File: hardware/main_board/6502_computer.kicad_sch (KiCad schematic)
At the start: 54 parts, among them J1 Conn_02x20_Odd_Even, J2 Conn_01x40_Socket, J3 Conn_01x40_Socket, J4 Conn_01x02_Pin, J6 DE9_Pins, J7 Mini-DIN-6, J8 Conn_01x12_Pin, SW1 SW_Push, U1 6502, U11 74HC595, U12 74HC138, U13 6522, U15 MAX232, U16 6551, U17 74HC595, U18 74HC14, U4 HM62256BLP, U8 74HC00, U9 28C256, Y1 CXO_DIP8, Y3 1.8432MHz

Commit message: Adds stuff
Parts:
- J6: footprint Connector_Dsub:DSUB-9_Pins_Horizontal_P2.77x2.84mm_EdgePinOffset7.70mm_Housed_MountingHolesOffset9.12mm -> Connector_Dsub:DSUB-9_Socket_Horizontal_P2.77x2.84mm_EdgePinOffset7.70mm_Housed_MountingHolesOffset9.12mm
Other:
- note added: "!!!!!!!!!CS2B!!!!!!!!"
- note added: "!!!!!!!!!RESB!!!!!!!!"
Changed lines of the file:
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@@
 		(rev "0")
 	)
+	(text "!!!!!!!!!CS2B!!!!!!!!"
+		(exclude_from_sim no)
+		(at 381.254 186.182 0)
+		(effects
+			(font
+				(size 2.54 2.54)
+				(thickness 0.254)
+				(bold yes)
+			)
+		)
+	)
 	(text "UART"
 		(exclude_from_sim no)
@@
 	(text "Keyboard \nlogic"
 		(exclude_from_sim no)
-		(at 281.94 214.376 0)
+		(at 284.226 217.17 0)
+		(effects
+			(font
+				(size 2.54 2.54)
+			)
+		)
+	)
+	(text "!!!!!!!!!RESB!!!!!!!!"
+		(exclude_from_sim no)
+		(at 345.44 46.228 0)
 		(effects
 			(font
 				(size 2.54 2.54)
+				(thickness 0.254)
+				(bold yes)
 			)
 		)
@@
 			)
 		)
-		(property "Footprint" "Connector_Dsub:DSUB-9_Pins_Horizontal_P2.77x2.84mm_EdgePinOffset7.70mm_Housed_MountingHolesOffset9.12mm"
+		(property "Footprint" "Connector_Dsub:DSUB-9_Socket_Horizontal_P2.77x2.84mm_EdgePinOffset7.70mm_Housed_MountingHolesOffset9.12mm"
 			(at 273.05 20.32 0)
 			(effects

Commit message: updated readme
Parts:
- R1, R2, R3, R6, R7, R8: footprint Resistor_THT:R_Axial_DIN0207_L6.3mm_D2.5mm_P7.62mm_Horizontal -> Resistor_THT:R_Axial_DIN0207_L6.3mm_D2.5mm_P10.16mm_Horizontal
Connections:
- net GND: no longer J1.2 (Pin_2), J1.31 (Pin_31), J2.2 (Pin_2), J2.37 (Pin_37), J2.38 (Pin_38), J3.2 (Pin_2), J3.37 (Pin_37), J3.38 (Pin_38)
- no-connect marks 40 -> 48
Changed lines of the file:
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@@
 	)
 	(junction
-		(at 106.68 265.43)
-		(diameter 0)
-		(color 0 0 0 0)
-	)
-	(junction
 		(at 270.51 161.29)
 		(diameter 0)
@@
 	)
 	(junction
-		(at 152.4 175.26)
-		(diameter 0)
-		(color 0 0 0 0)
-	)
-	(junction
 		(at 236.22 86.36)
 		(diameter 0)
@@
 	)
 	(junction
-		(at 106.68 267.97)
-		(diameter 0)
-		(color 0 0 0 0)
-	)
-	(junction
 		(at 161.29 49.53)
 		(diameter 0)
@@
 	)
 	(junction
-		(at 106.68 176.53)
-		(diameter 0)
-		(color 0 0 0 0)
-	)
-	(junction
 		(at 292.1 78.74)
 		(diameter 0)
@@
 	)
 	(junction
-		(at 77.47 176.53)
-		(diameter 0)
-		(color 0 0 0 0)
-	)
-	(junction
 		(at 229.87 144.78)
 		(diameter 0)
@@
 	)
 	(junction
-		(at 152.4 214.63)
-		(diameter 0)
-		(color 0 0 0 0)
-	)
-	(junction
 		(at 72.39 31.75)
 		(diameter 0)
@@
 	)
 	(junction
-		(at 77.47 267.97)
-		(diameter 0)
-		(color 0 0 0 0)
-	)
-	(junction
-		(at 77.47 265.43)
-		(diameter 0)
-		(color 0 0 0 0)
-	)
-	(junction
 		(at 39.37 116.84)
 		(diameter 0)
@@
 	)
 	(no_connect
+		(at 106.68 179.07)
+	)
+	(no_connect
 		(at 280.67 151.13)
 	)
@@
 	)
 	(no_connect
+		(at 106.68 270.51)
+	)
+	(no_connect
 		(at 74.93 134.62)
 	)
@@
 	)
 	(no_connect
+		(at 77.47 267.97)
+	)
+	(no_connect
 		(at 275.59 27.94)
 	)
@@
 	)
 	(no_connect
+		(at 152.4 217.17)
+	)
+	(no_connect
 		(at 77.47 273.05)
 	)
 	(no_connect
+		(at 77.47 270.51)
+	)
+	(no_connect
 		(at 71.12 68.58)
 	)
@@
 	)
 	(no_connect
+		(at 106.68 267.97)
+	)
+	(no_connect
 		(at 207.01 223.52)
 	)
 	(no_connect
+		(at 165.1 179.07)
+	)
+	(no_connect
 		(at 377.19 238.76)
 	)
+	(no_connect
+		(at 77.47 179.07)
+	)
 	(bus_entry
 		(at 377.19 160.02)
@@
 		)
 	)
-	(wire
-		(pts
-			(xy 106.68 265.43) (xy 106.68 267.97)
-		)
-		(stroke
-			(width 0)
-			(type default)
-		)
-	)
 	(bus
 		(pts
@@
 		)
 	)
-	(wire
-		(pts
-			(xy 152.4 214.63) (xy 152.4 217.17)
-		)
-		(stroke
-			(width 0)
-			(type default)
-		)
-	)
 	(bus
 		(pts
@@
 	(wire
 		(pts
-			(xy 165.1 179.07) (xy 165.1 175.26)
-		)
-		(stroke
-			(width 0)
-			(type default)
-		)
-	)
-	(wire
-		(pts
 			(xy 217.17 204.47) (xy 179.07 204.47)
 		)
@@
 	(wire
 		(pts
-			(xy 77.47 173.99) (xy 77.47 176.53)
-		)
-		(stroke
-			(width 0)
-			(type default)
-		)
-	)
-	(wire
-		(pts
 			(xy 330.2 67.31) (xy 341.63 67.31)
 		)
@@
 	(wire
 		(pts
-			(xy 106.68 267.97) (xy 106.68 270.51)
-		)
-		(stroke
-			(width 0)
-			(type default)
-		)
-	)
-	(wire
-		(pts
 			(xy 36.83 93.98) (xy 48.26 93.98)
 		)
@@
 	(wire
 		(pts
-			(xy 77.47 267.97) (xy 77.47 270.51)
-		)
-		(stroke
-			(width 0)
-			(type default)
-		)
-	)
-	(wire
-		(pts
 			(xy 100.33 255.27) (xy 106.68 255.27)
 		)
@@
 	(wire
 		(pts
-			(xy 100.33 270.51) (xy 100.33 275.59)
+			(xy 100.33 274.32) (xy 100.33 275.59)
 		)
 		(stroke
@@
 		)
 	)
-	(bus
+	(wire
 		(pts
-			(xy 344.17 72.39) (xy 344.17 74.93)
+			(xy 106.68 173.99) (xy 106.68 176.53)
 		)
 		(stroke
@@
 		)
 	)
-	(wire
+	(bus
 		(pts
-			(xy 187.96 147.32) (xy 194.31 147.32)
+			(xy 344.17 72.39) (xy 344.17 74.93)
 		)
 		(stroke
@@
 	(wire
 		(pts
-			(xy 259.08 128.27) (xy 270.51 128.27)
+			(xy 187.96 147.32) (xy 194.31 147.32)
 		)
 		(stroke
@@
 	(wire
 		(pts
-			(xy 229.87 130.81) (xy 229.87 133.35)
+			(xy 259.08 128.27) (xy 270.51 128.27)
 		)
 		(stroke
@@
 	(wire
 		(pts
-			(xy 106.68 173.99) (xy 106.68 176.53)
+			(xy 229.87 130.81) (xy 229.87 133.35)
 		)
 		(stroke
@@
 	(wire
 		(pts
+			(xy 77.47 173.99) (xy 77.47 176.53)
+		)
+		(stroke
+			(width 0)
+			(type default)
+		)
+	)
+	(wire
+		(pts
 			(xy 67.31 204.47) (xy 77.47 204.47)
 		)
@@
 	(wire
 		(pts
-			(xy 77.47 176.53) (xy 77.47 179.07)
-		)
-		(stroke
-			(width 0)
-			(type default)
-		)
-	)
-	(wire
-		(pts
 			(xy 236.22 86.36) (xy 257.81 86.36)
 		)
@@
 	(wire
 		(pts
-			(xy 106.68 176.53) (xy 106.68 179.07)
-		)
-		(stroke
-			(width 0)
-			(type default)
-		)
-	)
-	(wire
-		(pts
 			(xy 224.79 226.06) (xy 224.79 237.49)
 		)
@@
 	(wire
 		(pts
-			(xy 77.47 265.43) (xy 77.47 267.97)
-		)
-		(stroke
-			(width 0)
-			(type default)
-		)
-	)
-	(wire
-		(pts
 			(xy 148.59 102.87) (xy 148.59 110.49)
 		)
@@
 		)
 	)
-	(wire
-		(pts
-			(xy 152.4 175.26) (xy 165.1 175.26)
-		)
-		(stroke
-			(width 0)
-			(type default)
-		)
-	)
 	(bus
 		(pts
@@
 			)
 		)
-		(property "Footprint" "Resistor_THT:R_Axial_DIN0207_L6.3mm_D2.5mm_P7.62mm_Horizontal"
+		(property "Footprint" "Resistor_THT:R_Axial_DIN0207_L6.3mm_D2.5mm_P10.16mm_Horizontal"
 			(at 40.132 55.88 90)
 			(effects
@@
 			)
 		)
-		(property "Footprint" "Resistor_THT:R_Axial_DIN0207_L6.3mm_D2.5mm_P7.62mm_Horizontal"
+		(property "Footprint" "Resistor_THT:R_Axial_DIN0207_L6.3mm_D2.5mm_P10.16mm_Horizontal"
 			(at 19.812 55.88 90)
 			(effects
@@
 			)
 		)
-		(property "Footprint" "Resistor_THT:R_Axial_DIN0207_L6.3mm_D2.5mm_P7.62mm_Horizontal"
+		(property "Footprint" "Resistor_THT:R_Axial_DIN0207_L6.3mm_D2.5mm_P10.16mm_Horizontal"
 			(at 29.972 55.88 90)
 			(effects
@@
 			)
 		)
-		(property "Footprint" "Resistor_THT:R_Axial_DIN0207_L6.3mm_D2.5mm_P7.62mm_Horizontal"
+		(property "Footprint" "Resistor_THT:R_Axial_DIN0207_L6.3mm_D2.5mm_P10.16mm_Horizontal"
 			(at 98.552 29.21 90)
 			(effects
@@
 			)
 		)
-		(property "Footprint" "Resistor_THT:R_Axial_DIN0207_L6.3mm_D2.5mm_P7.62mm_Horizontal"
+		(property "Footprint" "Resistor_THT:R_Axial_DIN0207_L6.3mm_D2.5mm_P10.16mm_Horizontal"
 			(at 45.212 27.94 90)
 			(effects
@@
 	(symbol
 		(lib_id "power:VDD")
-		(at 100.33 270.51 0)
+		(at 100.33 274.32 0)
 		(unit 1)
 		(exclude_from_sim no)
@@
 		(dnp no)
 		(property "Reference" "#PWR045"
-			(at 100.33 274.32 0)
+			(at 100.33 278.13 0)
 			(effects
 				(font
@@
 		)
 		(property "Value" "VDD"
-			(at 97.282 270.002 0)
+			(at 97.282 273.812 0)
 			(effects
 				(font
@@
 		)
 		(property "Footprint" ""
-			(at 100.33 270.51 0)
+			(at 100.33 274.32 0)
 			(effects
 				(font
@@
 		)
 		(property "Datasheet" ""
-			(at 100.33 270.51 0)
+			(at 100.33 274.32 0)
 			(effects
 				(font
@@
 		)
 		(property "Description" "Power symbol creates a global label with name \"VDD\""
-			(at 100.33 270.51 0)
+			(at 100.33 274.32 0)
 			(effects
 				(font
@@
 			)
 		)
-		(property "Footprint" "Resistor_THT:R_Axial_DIN0207_L6.3mm_D2.5mm_P7.62mm_Horizontal"
+		(property "Footprint" "Resistor_THT:R_Axial_DIN0207_L6.3mm_D2.5mm_P10.16mm_Horizontal"
 			(at 248.92 227.838 90)
 			(effects

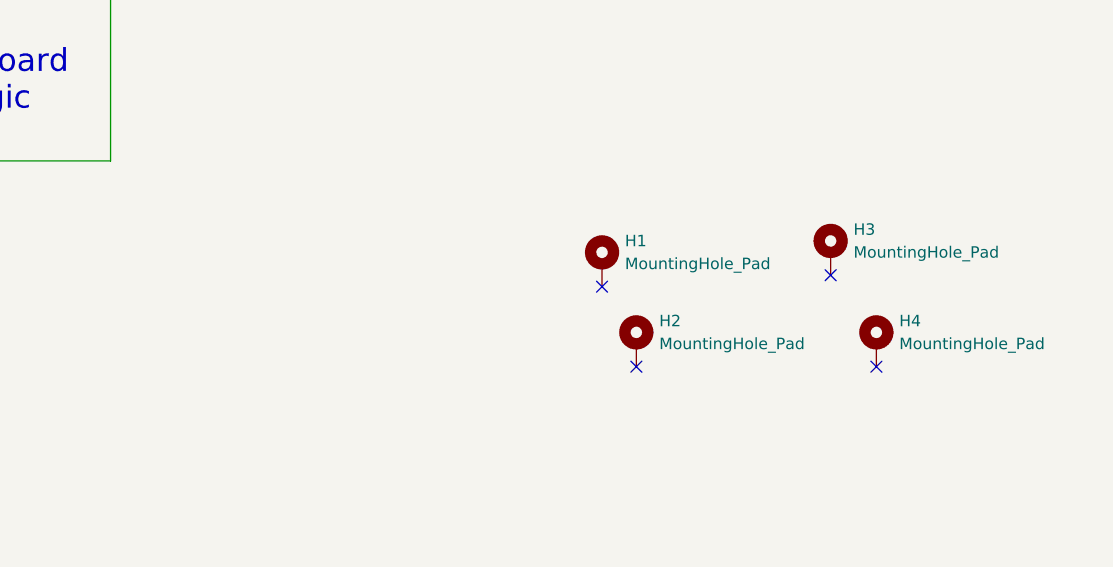
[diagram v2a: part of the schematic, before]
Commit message: replace load with rx
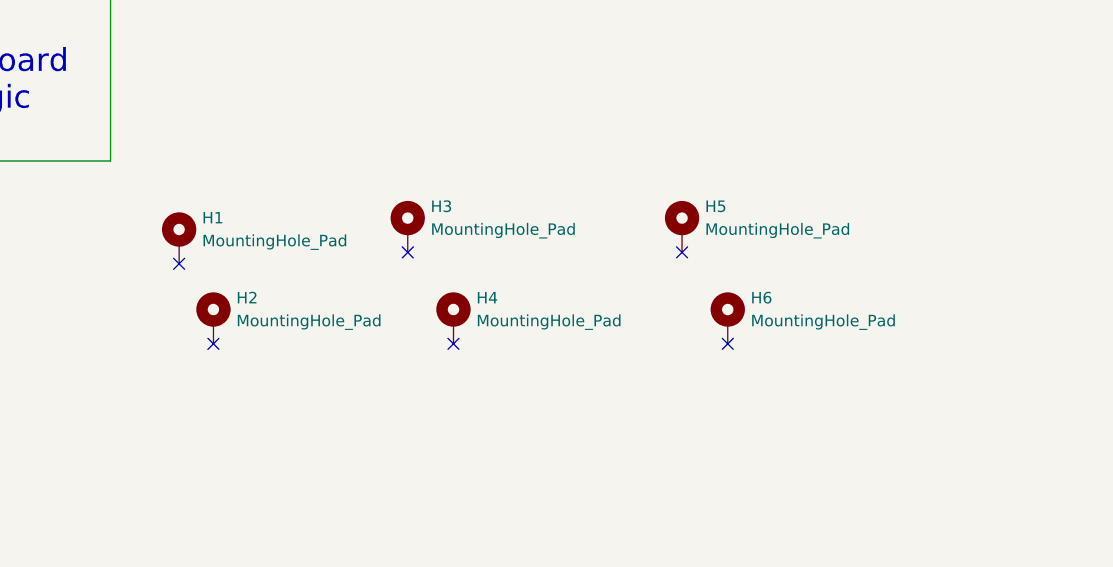
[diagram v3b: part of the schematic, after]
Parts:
- added H5, H6: MountingHole_Pad, MountingHole:MountingHole_3.2mm_M3_ISO7380_Pad, symbol Mechanical:MountingHole_Pad
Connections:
- no-connect marks 48 -> 50
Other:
- moved on the sheet: H1, H2, H3, H4
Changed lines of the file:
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@@
 	)
 	(no_connect
-		(at 351.79 240.03)
+		(at 304.8 237.49)
 	)
 	(no_connect
@@
 	)
 	(no_connect
-		(at 355.6 248.92)
+		(at 308.61 246.38)
 	)
 	(no_connect
@@
 	)
 	(no_connect
+		(at 360.68 236.22)
+	)
+	(no_connect
 		(at 152.4 219.71)
 	)
@@
 	)
 	(no_connect
+		(at 365.76 246.38)
+	)
+	(no_connect
 		(at 48.26 68.58)
 	)
@@
 	)
 	(no_connect
-		(at 382.27 248.92)
+		(at 335.28 246.38)
 	)
 	(no_connect
@@
 	)
 	(no_connect
-		(at 377.19 238.76)
+		(at 330.2 236.22)
 	)
 	(no_connect
@@
 	)
 	(symbol
+		(lib_id "Mechanical:MountingHole_Pad")
+		(at 360.68 233.68 0)
+		(unit 1)
+		(exclude_from_sim no)
+		(in_bom no)
+		(on_board yes)
+		(dnp no)
+		(fields_autoplaced yes)
+		(property "Reference" "H5"
+			(at 363.22 231.1399 0)
+			(effects
+				(font
+					(size 1.27 1.27)
+				)
+				(justify left)
+			)
+		)
+		(property "Value" "MountingHole_Pad"
+			(at 363.22 233.6799 0)
+			(effects
+				(font
+					(size 1.27 1.27)
+				)
+				(justify left)
+			)
+		)
+		(property "Footprint" "MountingHole:MountingHole_3.2mm_M3_ISO7380_Pad"
+			(at 360.68 233.68 0)
+			(effects
+				(font
+					(size 1.27 1.27)
+				)
+				(hide yes)
+			)
+		)
+		(property "Datasheet" "~"
+			(at 360.68 233.68 0)
+			(effects
+				(font
+					(size 1.27 1.27)
+				)
+				(hide yes)
+			)
+		)
+		(property "Description" "Mounting Hole with connection"
+			(at 360.68 233.68 0)
+			(effects
+				(font
+					(size 1.27 1.27)
+				)
+				(hide yes)
+			)
+		)
+		(pin "1"
+		)
+		(instances
+			(project "6502_computer"
+				(path "/12aa21c8-f5ca-498b-99d6-b9ebca65be14"
+					(reference "H5")
+					(unit 1)
+				)
+			)
+		)
+	)
+	(symbol
 		(lib_id "power:GND")
 		(at 140.97 175.26 0)
@@
 	(symbol
 		(lib_id "Mechanical:MountingHole_Pad")
-		(at 382.27 246.38 0)
+		(at 335.28 243.84 0)
 		(unit 1)
 		(exclude_from_sim no)
@@
 		(fields_autoplaced yes)
 		(property "Reference" "H4"
-			(at 384.81 243.8399 0)
+			(at 337.82 241.2999 0)
 			(effects
 				(font
@@
 		)
 		(property "Value" "MountingHole_Pad"
-			(at 384.81 246.3799 0)
+			(at 337.82 243.8399 0)
 			(effects
 				(font
@@
 		)
 		(property "Footprint" "MountingHole:MountingHole_3.2mm_M3_ISO7380_Pad"
-			(at 382.27 246.38 0)
+			(at 335.28 243.84 0)
 			(effects
 				(font
@@
 		)
 		(property "Datasheet" "~"
-			(at 382.27 246.38 0)
+			(at 335.28 243.84 0)
 			(effects
 				(font
@@
 		)
 		(property "Description" "Mounting Hole with connection"
-			(at 382.27 246.38 0)
+			(at 335.28 243.84 0)
 			(effects
 				(font
@@
 	(symbol
 		(lib_id "Mechanical:MountingHole_Pad")
-		(at 377.19 236.22 0)
+		(at 330.2 233.68 0)
 		(unit 1)
 		(exclude_from_sim no)
@@
 		(fields_autoplaced yes)
 		(property "Reference" "H3"
-			(at 379.73 233.6799 0)
+			(at 332.74 231.1399 0)
 			(effects
 				(font
@@
 		)
 		(property "Value" "MountingHole_Pad"
-			(at 379.73 236.2199 0)
+			(at 332.74 233.6799 0)
 			(effects
 				(font
@@
 		)
 		(property "Footprint" "MountingHole:MountingHole_3.2mm_M3_ISO7380_Pad"
-			(at 377.19 236.22 0)
+			(at 330.2 233.68 0)
 			(effects
 				(font
@@
 		)
 		(property "Datasheet" "~"
-			(at 377.19 236.22 0)
+			(at 330.2 233.68 0)
 			(effects
 				(font
@@
 		)
 		(property "Description" "Mounting Hole with connection"
-			(at 377.19 236.22 0)
+			(at 330.2 233.68 0)
 			(effects
 				(font
@@
 	(symbol
 		(lib_id "Mechanical:MountingHole_Pad")
-		(at 351.79 237.49 0)
+		(at 304.8 234.95 0)
 		(unit 1)
 		(exclude_from_sim no)
@@
 		(fields_autoplaced yes)
 		(property "Reference" "H1"
-			(at 354.33 234.9499 0)
+			(at 307.34 232.4099 0)
 			(effects
 				(font
@@
 		)
 		(property "Value" "MountingHole_Pad"
-			(at 354.33 237.4899 0)
+			(at 307.34 234.9499 0)
 			(effects
 				(font
@@
 		)
 		(property "Footprint" "MountingHole:MountingHole_3.2mm_M3_ISO7380_Pad"
-			(at 351.79 237.49 0)
+			(at 304.8 234.95 0)
 			(effects
 				(font
@@
 		)
 		(property "Datasheet" "~"
-			(at 351.79 237.49 0)
+			(at 304.8 234.95 0)
 			(effects
 				(font
@@
 		)
 		(property "Description" "Mounting Hole with connection"
-			(at 351.79 237.49 0)
+			(at 304.8 234.95 0)
 			(effects
 				(font
@@
 	)
 	(symbol
+		(lib_id "Mechanical:MountingHole_Pad")
+		(at 365.76 243.84 0)
+		(unit 1)
+		(exclude_from_sim no)
+		(in_bom no)
+		(on_board yes)
+		(dnp no)
+		(fields_autoplaced yes)
+		(property "Reference" "H6"
+			(at 368.3 241.2999 0)
+			(effects
+				(font
+					(size 1.27 1.27)
+				)
+				(justify left)
+			)
+		)
+		(property "Value" "MountingHole_Pad"
+			(at 368.3 243.8399 0)
+			(effects
+				(font
+					(size 1.27 1.27)
+				)
+				(justify left)
+			)
+		)
+		(property "Footprint" "MountingHole:MountingHole_3.2mm_M3_ISO7380_Pad"
+			(at 365.76 243.84 0)
+			(effects
+				(font
+					(size 1.27 1.27)
+				)
+				(hide yes)
+			)
+		)
+		(property "Datasheet" "~"
+			(at 365.76 243.84 0)
+			(effects
+				(font
+					(size 1.27 1.27)
+				)
+				(hide yes)
+			)
+		)
+		(property "Description" "Mounting Hole with connection"
+			(at 365.76 243.84 0)
+			(effects
+				(font
+					(size 1.27 1.27)
+				)
+				(hide yes)
+			)
+		)
+		(pin "1"
+		)
+		(instances
+			(project "6502_computer"
+				(path "/12aa21c8-f5ca-498b-99d6-b9ebca65be14"
+					(reference "H6")
+					(unit 1)
+				)
+			)
+		)
+	)
+	(symbol
 		(lib_id "power:GND")
 		(at 72.39 34.29 0)
@@
 	(symbol
 		(lib_id "Mechanical:MountingHole_Pad")
-		(at 355.6 246.38 0)
+		(at 308.61 243.84 0)
 		(unit 1)
 		(exclude_from_sim no)
@@
 		(fields_autoplaced yes)
 		(property "Reference" "H2"
-			(at 358.14 243.8399 0)
+			(at 311.15 241.2999 0)
 			(effects
 				(font
@@
 		)
 		(property "Value" "MountingHole_Pad"
-			(at 358.14 246.3799 0)
+			(at 311.15 243.8399 0)
 			(effects
 				(font
@@
 		)
 		(property "Footprint" "MountingHole:MountingHole_3.2mm_M3_ISO7380_Pad"
-			(at 355.6 246.38 0)
+			(at 308.61 243.84 0)
 			(effects
 				(font
@@
 		)
 		(property "Datasheet" "~"
-			(at 355.6 246.38 0)
+			(at 308.61 243.84 0)
 			(effects
 				(font
@@
 		)
 		(property "Description" "Mounting Hole with connection"
-			(at 355.6 246.38 0)
+			(at 308.61 243.84 0)
 			(effects
 				(font

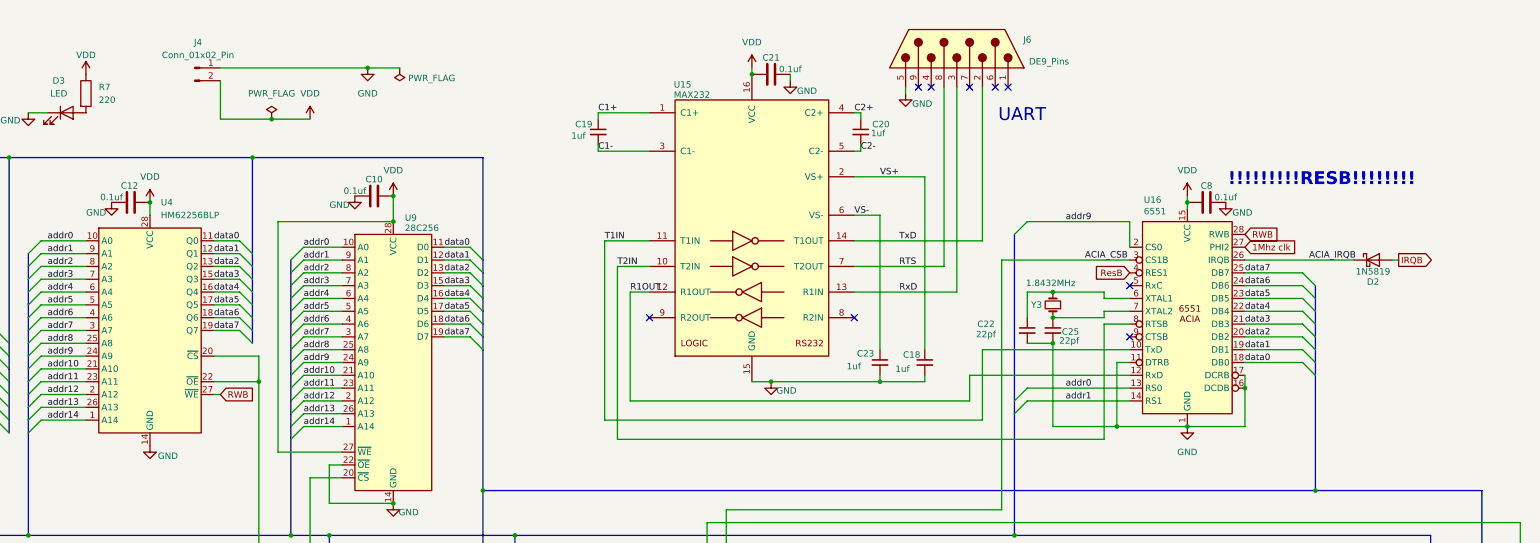
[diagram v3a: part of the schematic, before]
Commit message: Updated gitignore
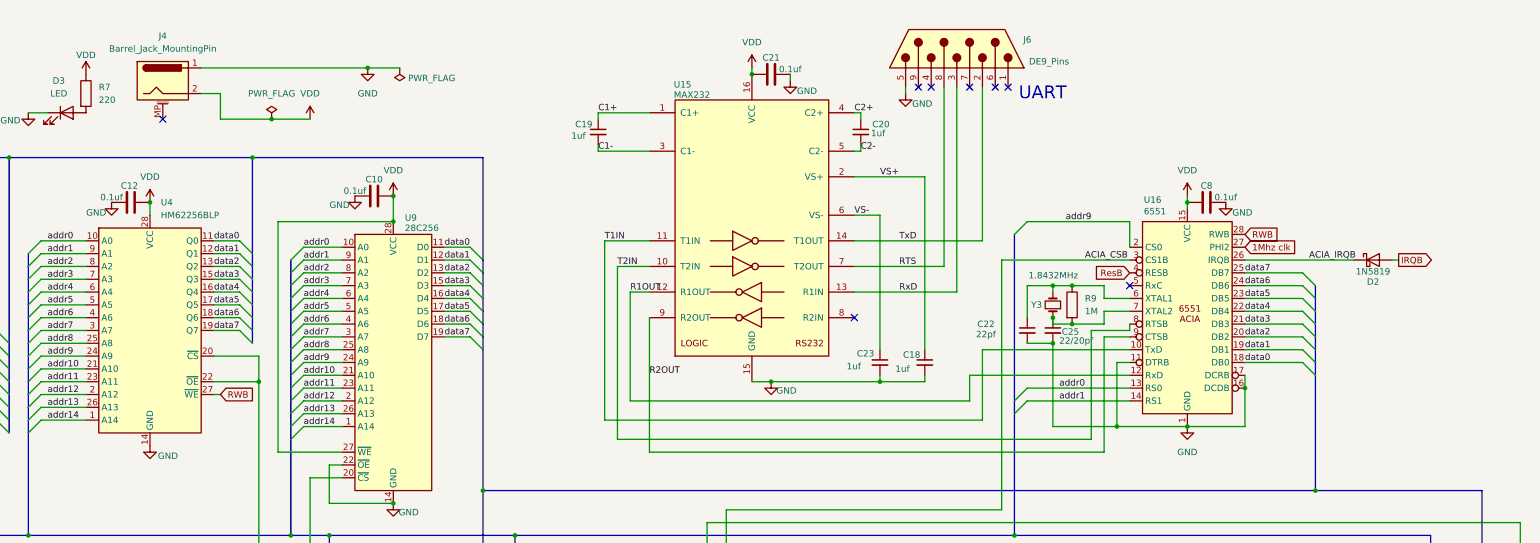
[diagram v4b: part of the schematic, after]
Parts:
- removed J4: Conn_01x02_Pin, Connector_PinHeader_2.54mm:PinHeader_1x02_P2.54mm_Horizontal, symbol Connector:Conn_01x02_Pin
- added J4: Barrel_Jack_MountingPin, Connector_BarrelJack:BarrelJack_Horizontal, symbol Connector:Barrel_Jack_MountingPin
- added R9: 1M, Resistor_THT:R_Axial_DIN0207_L6.3mm_D2.5mm_P10.16mm_Horizontal, symbol Device:R
- C25: value 22pf -> 22/20pf
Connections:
- net GND: now also J4.1
- net VDD: now also J4.2
- net at C25.1, U16.7 (XTAL2), Y3.1: now also R9.2
- net at C22.1, U16.6 (XTAL1), Y3.2: now also R9.1
- net R2OUT: now reaches U15.9 (R2OUT)
- net R2OUT: now also U16.9 (CTSB)
- no-connect marks 50 -> 49
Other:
- note removed: "!!!!!!!!!RESB!!!!!!!!"
